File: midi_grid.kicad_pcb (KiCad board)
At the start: 2 copper layers, 275 x 200 mm, 311 parts, among them J1 USB_OTG, J2 3.5mm jack, J3 3.5mm jack, J4 Conn_01x04_Male, Q1 BSS83P, Q10 BSS83P, Q11 BSS83P, Q12 BSS83P, Q13 BSS83P, Q14 BSS83P, Q15 BSS83P, Q16 BSS83P, Q17 BSS83P, Q18 BSS83P, Q19 BSS83P, Q2 BSS83P, Q20 BSS83P, Q21 NX7002AK, Q22 NX7002AK, Q23 NX7002AK, Q24 NX7002AK, Q25 NX7002AK, Q26 NX7002AK, Q27 NX7002AK, Q28 NX7002AK, Q29 NX7002AK, Q3 BSS83P, Q30 NX7002AK, Q31 NX7002AK, Q32 NX7002AK, Q33 NX7002AK, Q34 NX7002AK, Q4 BSS83P, Q5 BSS83P, Q6 BSS83P, Q7 BSS83P, Q8 BSS83P, Q9 BSS83P, SW1 Button_matrix_4x4, SW10 SW_Push, SW11 SW_Push, SW12 SW_Push, SW13 SW_Push, SW14 SW_Push, SW15 SW_Push, SW16 SW_Push, SW17 SW_Push, SW18 SW_Push, SW19 SW_Push, SW2 Button_matrix_4x4, SW20 SW_Push, SW21 SW_Push, SW22 SW_Push, SW23 SW_Push, SW24 SW_Push, SW25 EC12E24204A9, SW26 EC12E24204A9, SW3 Button_matrix_4x4, SW4 Button_matrix_4x4, SW5 SW_Push, SW6 SW_Push, SW7 SW_Push, SW8 SW_Push, SW9 SW_Push, U1 74HC138, U2 74HC138, U3 74HC138, U4 USBUF, U5 STM32F411RCT6, U6 LD1117STR, U7 LTV-357T, Y1 8MHz

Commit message: multiple schematic and pcb changes
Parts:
- removed R35, R36, R37, R38: 10K, Resistors_SMD:R_0603
- added TP1: TEST, Connectors_TestPoints:Test_Point_Pad_d4.0mm, F.Cu at (176.0, 258.5)
- added TP2: TEST, Connectors_TestPoints:Test_Point_Pad_d4.0mm, F.Cu at (182.0, 254.0)
- added TP3: TEST, Connectors_TestPoints:Test_Point_Pad_d4.0mm, F.Cu at (188.5, 255.5)
- added TP4: TEST, Connectors_TestPoints:Test_Point_Pad_d4.0mm, F.Cu at (195.0, 257.0)
- added TP5: TEST, Connectors_TestPoints:Test_Point_Pad_d4.0mm, F.Cu at (201.0, 261.0)
- C14, C15, C2, R52, R53, R54, R55: moved to B.Cu
- moved R28 192.4 mm to (276.0, 96.0), turned to 270 degrees
- moved Q25 188.6 mm to (273.5, 85.5), turned to 180 degrees
- moved R25 187.1 mm to (276.0, 85.5), turned to 270 degrees
- moved R55 178.1 mm to (269.5, 96.0)
- moved Q26 175.0 mm to (273.5, 89.0), turned to 180 degrees
- moved R54 173.8 mm to (269.5, 92.5)
- moved R53 173.3 mm to (269.5, 89.0)
- moved R52 167.7 mm to (269.5, 85.5)
- moved Q28 156.9 mm to (273.5, 96.0), turned to 180 degrees
- moved R27 153.5 mm to (276.0, 92.5), turned to 270 degrees
- moved R26 150.3 mm to (276.0, 89.0), turned to 270 degrees
- moved Q27 149.4 mm to (273.5, 92.5), turned to 180 degrees
- moved C2 136.3 mm to (263.5, 110.5)
- moved C15 102.9 mm to (306.0, 116.0), turned to 270 degrees
- moved C14 101.5 mm to (301.5, 116.0), turned to 270 degrees
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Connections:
- net /grid/BLUE1 renamed /grid/PWM_BLUE1
- net /grid/BLUE2 renamed /grid/PWM_BLUE2
- net /grid/BLUE3 renamed /grid/PWM_BLUE3
- net /grid/BLUE4 renamed /grid/PWM_BLUE4
- net /grid/BUTTON4 renamed /mcu/GRID_BUTTON4
- net /grid/GREEN1 renamed /grid/PWM_GREEN1
- net /grid/GREEN2 renamed /grid/PWM_GREEN2
- net /grid/GREEN3 renamed /grid/PWM_GREEN3
- net /grid/GREEN4 renamed /grid/PWM_GREEN4
- net /mcu/PWM_RED1 renamed /grid/PWM_RED1
- net /mcu/PWM_RED2 renamed /grid/PWM_RED2
- net /mcu/PWM_RED3 renamed /grid/PWM_RED3
- net /mcu/PWM_RED4 renamed /grid/PWM_RED4
- U5 pad 10: /grid/BUTTON3 -> /mcu/GRID_BUTTON3
- U5 pad 2: Net-(U5-Pad2) -> /digital_io/BUTTON2
- U5 pad 24: /digital_io/BUTTON1 -> Net-(TP4-Pad1)
- U5 pad 25: /digital_io/BUTTON2 -> Net-(TP5-Pad1)
- U5 pad 53: Net-(U5-Pad53) -> /digital_io/BUTTON1
- U5 pad 8: /grid/BUTTON1 -> /mcu/GRID_BUTTON1
- U5 pad 9: /grid/BUTTON2 -> /mcu/GRID_BUTTON2
- Y1 pad 2: /mcu/XTAL2 -> GND
- Y1 pad 3: (no net) -> /mcu/XTAL2
- Y1 pad 4: (no net) -> GND
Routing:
- net /mcu/COL3: track 0.00 -> 63.8 mm, vias 0 -> 1
- net /grid/G8: track 1.58 -> 50.0 mm, vias 0 -> 2
- net /grid/G7: track 1.58 -> 48.2 mm, vias 0 -> 2
- net +5V: track 235.4 -> 277.7 mm, vias 2 -> 4
- net /grid/G6: track 1.58 -> 39.9 mm, vias 0 -> 2
- net /grid/G5: track 1.58 -> 36.3 mm, vias 0 -> 2
- net /grid/PWM_GREEN1: track 0.00 -> 17.8 mm
- net /grid/PWM_GREEN2: track 0.00 -> 17.1 mm
- net /grid/PWM_GREEN4: track 0.00 -> 16.4 mm
- net /grid/PWM_GREEN3: track 0.00 -> 16.1 mm
- net /mcu/COL2: track 0.00 -> 8.68 mm
- net /mcu/COL1: track 0.00 -> 8.32 mm
- net (no net): track 0.00 -> 5.00 mm

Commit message: pcb in development
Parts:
- removed TP5: TEST, Connectors_TestPoints:Test_Point_Pad_d4.0mm
- added R35: 10K, Resistors_SMD:R_0603, B.Cu at (295.8, 93.0)
- added TP6: TEST, Connectors_TestPoints:Test_Point_Pad_d3.0mm, F.Cu at (205.0, 259.5)
- C10, C11, C12, C6, C7, C8, C9: moved to B.Cu
- TP1, TP2, TP3: footprint Connectors_TestPoints:Test_Point_Pad_d4.0mm -> Connectors_TestPoints:Test_Point_Pad_d3.0mm
- TP4: footprint Connectors_TestPoints:Test_Point_Pad_d4.0mm -> Connectors_TestPoints:Test_Point_Pad_d3.0mm; moved to B.Cu
- moved TP4 187.9 mm to (280.2, 89.5)
- moved C12 175.3 mm to (296.2, 97.2), turned to 90 degrees
- moved C10 174.2 mm to (308.2, 108.0)
- moved C8 98.0 mm to (304.8, 85.0)
- moved C7 94.2 mm to (304.2, 90.2)
- moved C11 91.6 mm to (300.8, 109.8)
- moved C6 89.8 mm to (297.0, 95.2), turned to 180 degrees
- moved C9 82.0 mm to (307.4, 87.6)
- moved C13 19.4 mm to (367.2, 41.8)
- moved R52 3.50 mm to (269.5, 89.0)
- moved Y1 2.70 mm to (304.2, 113.0)
- moved R53 2.50 mm to (269.5, 91.5)
- moved R54 1.50 mm to (269.5, 94.0)
- moved R55 0.50 mm to (269.5, 96.5)
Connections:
- D10 pad 1: /grid/BUTTON3 -> /grid/GRID_BUTTON3
- D100 pad 1: Net-(D100-Pad1) -> /grid/GRID_BUTTON4
- D102 pad 1: Net-(D100-Pad1) -> /grid/GRID_BUTTON4
- D104 pad 1: Net-(D100-Pad1) -> /grid/GRID_BUTTON4
- D106 pad 1: /grid/BUTTON3 -> /grid/GRID_BUTTON3
- D108 pad 1: /grid/BUTTON3 -> /grid/GRID_BUTTON3
- D110 pad 1: /grid/BUTTON3 -> /grid/GRID_BUTTON3
- D112 pad 1: /grid/BUTTON3 -> /grid/GRID_BUTTON3
- D114 pad 1: /grid/BUTTON2 -> /grid/GRID_BUTTON2
- D116 pad 1: /grid/BUTTON2 -> /grid/GRID_BUTTON2
- D118 pad 1: /grid/BUTTON2 -> /grid/GRID_BUTTON2
- D12 pad 1: /grid/BUTTON3 -> /grid/GRID_BUTTON3
- D120 pad 1: /grid/BUTTON2 -> /grid/GRID_BUTTON2
- D122 pad 1: /grid/BUTTON1 -> /grid/GRID_BUTTON1
- D124 pad 1: /grid/BUTTON1 -> /grid/GRID_BUTTON1
- D126 pad 1: /grid/BUTTON1 -> /grid/GRID_BUTTON1
- D128 pad 1: /grid/BUTTON1 -> /grid/GRID_BUTTON1
- D130 pad 1: Net-(D100-Pad1) -> /grid/GRID_BUTTON4
- D131 pad 1: Net-(D100-Pad1) -> /grid/GRID_BUTTON4
- D133 pad 1: /grid/BUTTON3 -> /grid/GRID_BUTTON3
- D135 pad 1: /grid/BUTTON3 -> /grid/GRID_BUTTON3
- D137 pad 1: /grid/BUTTON2 -> /grid/GRID_BUTTON2
- D138 pad 1: /grid/BUTTON2 -> /grid/GRID_BUTTON2
- D139 pad 1: /grid/BUTTON1 -> /grid/GRID_BUTTON1
- D14 pad 1: /grid/BUTTON3 -> /grid/GRID_BUTTON3
- D141 pad 1: /grid/BUTTON1 -> /grid/GRID_BUTTON1
- D143 pad 1: Net-(D100-Pad1) -> /grid/GRID_BUTTON4
- D145 pad 1: Net-(D100-Pad1) -> /grid/GRID_BUTTON4
- D147 pad 1: /grid/BUTTON3 -> /grid/GRID_BUTTON3
- D149 pad 1: /grid/BUTTON3 -> /grid/GRID_BUTTON3
- D151 pad 1: /grid/BUTTON2 -> /grid/GRID_BUTTON2
- D153 pad 1: /grid/BUTTON2 -> /grid/GRID_BUTTON2
- D155 pad 1: /grid/BUTTON1 -> /grid/GRID_BUTTON1
- D157 pad 1: /grid/BUTTON1 -> /grid/GRID_BUTTON1
- D16 pad 1: /grid/BUTTON3 -> /grid/GRID_BUTTON3
- D18 pad 1: /grid/BUTTON2 -> /grid/GRID_BUTTON2
- D2 pad 1: Net-(D100-Pad1) -> /grid/GRID_BUTTON4
- D20 pad 1: /grid/BUTTON2 -> /grid/GRID_BUTTON2
- D22 pad 1: /grid/BUTTON2 -> /grid/GRID_BUTTON2
- D24 pad 1: /grid/BUTTON2 -> /grid/GRID_BUTTON2
- D26 pad 1: /grid/BUTTON1 -> /grid/GRID_BUTTON1
- D28 pad 1: /grid/BUTTON1 -> /grid/GRID_BUTTON1
- D30 pad 1: /grid/BUTTON1 -> /grid/GRID_BUTTON1
- D32 pad 1: /grid/BUTTON1 -> /grid/GRID_BUTTON1
- D34 pad 1: Net-(D100-Pad1) -> /grid/GRID_BUTTON4
- D36 pad 1: Net-(D100-Pad1) -> /grid/GRID_BUTTON4
- D38 pad 1: Net-(D100-Pad1) -> /grid/GRID_BUTTON4
- D4 pad 1: Net-(D100-Pad1) -> /grid/GRID_BUTTON4
- D40 pad 1: Net-(D100-Pad1) -> /grid/GRID_BUTTON4
- D42 pad 1: /grid/BUTTON3 -> /grid/GRID_BUTTON3
- D44 pad 1: /grid/BUTTON3 -> /grid/GRID_BUTTON3
- D46 pad 1: /grid/BUTTON3 -> /grid/GRID_BUTTON3
- D48 pad 1: /grid/BUTTON3 -> /grid/GRID_BUTTON3
- D50 pad 1: /grid/BUTTON2 -> /grid/GRID_BUTTON2
- D52 pad 1: /grid/BUTTON2 -> /grid/GRID_BUTTON2
- D54 pad 1: /grid/BUTTON2 -> /grid/GRID_BUTTON2
- D56 pad 1: /grid/BUTTON2 -> /grid/GRID_BUTTON2
- D58 pad 1: /grid/BUTTON1 -> /grid/GRID_BUTTON1
- D6 pad 1: Net-(D100-Pad1) -> /grid/GRID_BUTTON4
- D60 pad 1: /grid/BUTTON1 -> /grid/GRID_BUTTON1
- D62 pad 1: /grid/BUTTON1 -> /grid/GRID_BUTTON1
- D64 pad 1: /grid/BUTTON1 -> /grid/GRID_BUTTON1
- D66 pad 1: Net-(D100-Pad1) -> /grid/GRID_BUTTON4
- D68 pad 1: Net-(D100-Pad1) -> /grid/GRID_BUTTON4
- D70 pad 1: Net-(D100-Pad1) -> /grid/GRID_BUTTON4
- D72 pad 1: Net-(D100-Pad1) -> /grid/GRID_BUTTON4
- D74 pad 1: /grid/BUTTON3 -> /grid/GRID_BUTTON3
- D76 pad 1: /grid/BUTTON3 -> /grid/GRID_BUTTON3
- D78 pad 1: /grid/BUTTON3 -> /grid/GRID_BUTTON3
- D8 pad 1: Net-(D100-Pad1) -> /grid/GRID_BUTTON4
- D80 pad 1: /grid/BUTTON3 -> /grid/GRID_BUTTON3
- D82 pad 1: /grid/BUTTON2 -> /grid/GRID_BUTTON2
- D84 pad 1: /grid/BUTTON2 -> /grid/GRID_BUTTON2
- D86 pad 1: /grid/BUTTON2 -> /grid/GRID_BUTTON2
- D88 pad 1: /grid/BUTTON2 -> /grid/GRID_BUTTON2
- D90 pad 1: /grid/BUTTON1 -> /grid/GRID_BUTTON1
- D92 pad 1: /grid/BUTTON1 -> /grid/GRID_BUTTON1
- D94 pad 1: /grid/BUTTON1 -> /grid/GRID_BUTTON1
- D96 pad 1: /grid/BUTTON1 -> /grid/GRID_BUTTON1
- D98 pad 1: Net-(D100-Pad1) -> /grid/GRID_BUTTON4
- U5 pad 10: /mcu/GRID_BUTTON3 -> /grid/GRID_BUTTON3
- U5 pad 11: /mcu/GRID_BUTTON4 -> /grid/GRID_BUTTON4
- U5 pad 2: /digital_io/BUTTON2 -> /digital_io/BUTTON1
- U5 pad 28: Net-(U5-Pad28) -> /digital_io/LCD_RESET
- U5 pad 29: /digital_io/LCD_DC -> /digital_io/LCD_CS
- U5 pad 3: /digital_io/ROTARY2_A -> /digital_io/ROTARY1_A
- U5 pad 33: /digital_io/LCD_CS -> /digital_io/LCD_DC
- U5 pad 39: /digital_io/LCD_RESET -> Net-(TP6-Pad1)
- U5 pad 4: /digital_io/ROTARY2_B -> /digital_io/ROTARY1_B
- U5 pad 51: /digital_io/ROTARY1_A -> /digital_io/ROTARY2_A
- U5 pad 52: /digital_io/ROTARY1_B -> /digital_io/ROTARY2_B
- U5 pad 53: /digital_io/BUTTON1 -> /digital_io/BUTTON2
- U5 pad 8: /mcu/GRID_BUTTON1 -> /grid/GRID_BUTTON1
- U5 pad 9: /mcu/GRID_BUTTON2 -> /grid/GRID_BUTTON2
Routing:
- net /grid/GRID_BUTTON1: track 0.00 -> 511.3 mm, vias 0 -> 3
- net /grid/BUTTON1: track 508.0 -> 0.00 mm, vias 3 -> 0
- net /grid/GRID_BUTTON3: track 0.00 -> 499.2 mm, vias 0 -> 3
- net /grid/BUTTON3: track 495.9 -> 0.00 mm, vias 3 -> 0
- net /grid/GRID_BUTTON2: track 0.00 -> 475.9 mm, vias 0 -> 3
- net /grid/BUTTON2: track 472.6 -> 0.00 mm, vias 3 -> 0
- net /grid/GRID_BUTTON4: track 0.00 -> 462.9 mm, vias 0 -> 3
- net Net-(D100-Pad1): track 459.6 -> 0.00 mm, vias 3 -> 0
- net GND: track 0.75 -> 26.7 mm, vias 1 -> 2
- net Net-(TP4-Pad1): track 0.00 -> 17.4 mm
- net /grid/PWM_GREEN1: track 17.8 -> 32.8 mm
- net /digital_io/LCD_RESET: track 0.00 -> 12.1 mm
- net /grid/PWM_GREEN2: track 17.1 -> 28.6 mm
- net /digital_io/LCD_CS: track 0.00 -> 8.71 mm
- net +3V3: track 8.59 -> 16.3 mm, vias 0 -> 1
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
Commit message: pcb development
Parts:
- Q33, R34, R60: moved to F.Cu
- R48, R49, R50, R51: moved to B.Cu
- moved R24 199.4 mm to (276.0, 96.0), turned to 270 degrees
- moved R49 172.9 mm to (269.5, 91.5)
- moved R51 172.6 mm to (269.5, 96.5)
- moved R48 171.2 mm to (269.5, 89.0)
- moved R50 170.3 mm to (269.5, 94.0)
- moved Q21 165.5 mm to (273.5, 85.5), turned to 180 degrees
- moved Q24 153.1 mm to (273.5, 96.0), turned to 180 degrees
- moved Q23 150.6 mm to (273.5, 92.5), turned to 180 degrees
- moved R22 150.1 mm to (276.0, 89.0), turned to 270 degrees
- moved R21 146.8 mm to (276.0, 85.5), turned to 270 degrees
- moved R23 145.0 mm to (276.0, 92.5), turned to 270 degrees
- moved Q22 142.4 mm to (273.5, 89.0), turned to 180 degrees
- moved U4 45.2 mm to (338.0, 91.5)
- moved Q25 25.0 mm to (273.2, 60.5)
- moved Q26 25.0 mm to (273.2, 64.0)
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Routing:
- net Net-(D121-Pad1): track 530.6 -> 683.8 mm, vias 0 -> 3
- net Net-(D1-Pad1): track 451.3 -> 587.3 mm, vias 0 -> 3
- net Net-(D105-Pad1): track 488.4 -> 620.5 mm, vias 0 -> 3
- net Net-(D113-Pad1): track 463.5 -> 569.9 mm, vias 0 -> 2
- net /mcu/USB_DP: track 0.00 -> 55.5 mm
- net /mcu/USB_DM: track 0.00 -> 54.9 mm
- net /grid/PWM_GREEN4: track 16.9 -> 51.9 mm
- net /grid/PWM_RED4: track 0.00 -> 34.5 mm
- net /grid/PWM_GREEN3: track 18.2 -> 52.0 mm
- net /grid/PWM_RED2: track 2.32 -> 34.6 mm
- net /grid/PWM_RED3: track 1.71 -> 33.0 mm
- net /grid/PWM_RED1: track 5.75 -> 36.3 mm
- net Net-(TP4-Pad1): track 17.4 -> 47.9 mm
- net GND: track 26.7 -> 53.7 mm, vias 2 -> 3
- net /mcu/USB_M: track 0.00 -> 25.9 mm, vias 0 -> 1
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
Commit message: commiting before bulk led schematic symbol change
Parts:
- C13, C3, R56, R57, R58, R59: moved to B.Cu
- R45: moved to F.Cu
- moved R58 242.0 mm to (397.2, 140.0)
- moved R57 241.8 mm to (397.5, 135.8)
- moved R56 222.5 mm to (397.8, 131.2)
- moved R59 196.7 mm to (397.2, 144.2)
- moved R45 138.9 mm to (305.0, 64.0)
- moved R33 108.7 mm to (347.0, 108.0)
- moved C13 93.9 mm to (296.2, 103.2), turned to 180 degrees
- moved C3 84.0 mm to (376.8, 80.8)
- moved R32 83.3 mm to (390.0, 144.5), turned to 90 degrees
- moved R31 81.8 mm to (390.0, 140.5), turned to 90 degrees
- moved R29 81.1 mm to (390.0, 131.5), turned to 90 degrees
- moved U3 78.1 mm to (378.8, 84.5)
- moved R30 77.9 mm to (390.0, 136.0), turned to 90 degrees
- moved SW22 58.8 mm to (295.0, 109.0), turned to 270 degrees
- moved Q32 58.7 mm to (392.5, 144.5)
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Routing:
- net Net-(D121-Pad4): track 536.3 -> 766.5 mm, vias 0 -> 3
- net Net-(D113-Pad4): track 468.9 -> 681.5 mm, vias 0 -> 3
- net Net-(D105-Pad4): track 492.1 -> 681.5 mm, vias 0 -> 3
- net Net-(D1-Pad4): track 456.8 -> 642.9 mm, vias 0 -> 3
- net /mcu/NRST: track 6.86 -> 10.9 mm
- net /digital_io/LCD_LIGHT: track 8.15 -> 10.9 mm
- net /grid/GRID_BUTTON2: track 478.7 -> 480.3 mm
- net /grid/GRID_BUTTON3: track 501.2 -> 502.5 mm
- net Net-(D105-Pad1): track 620.5 -> 621.2 mm
- net (no net): vias 6 -> 0

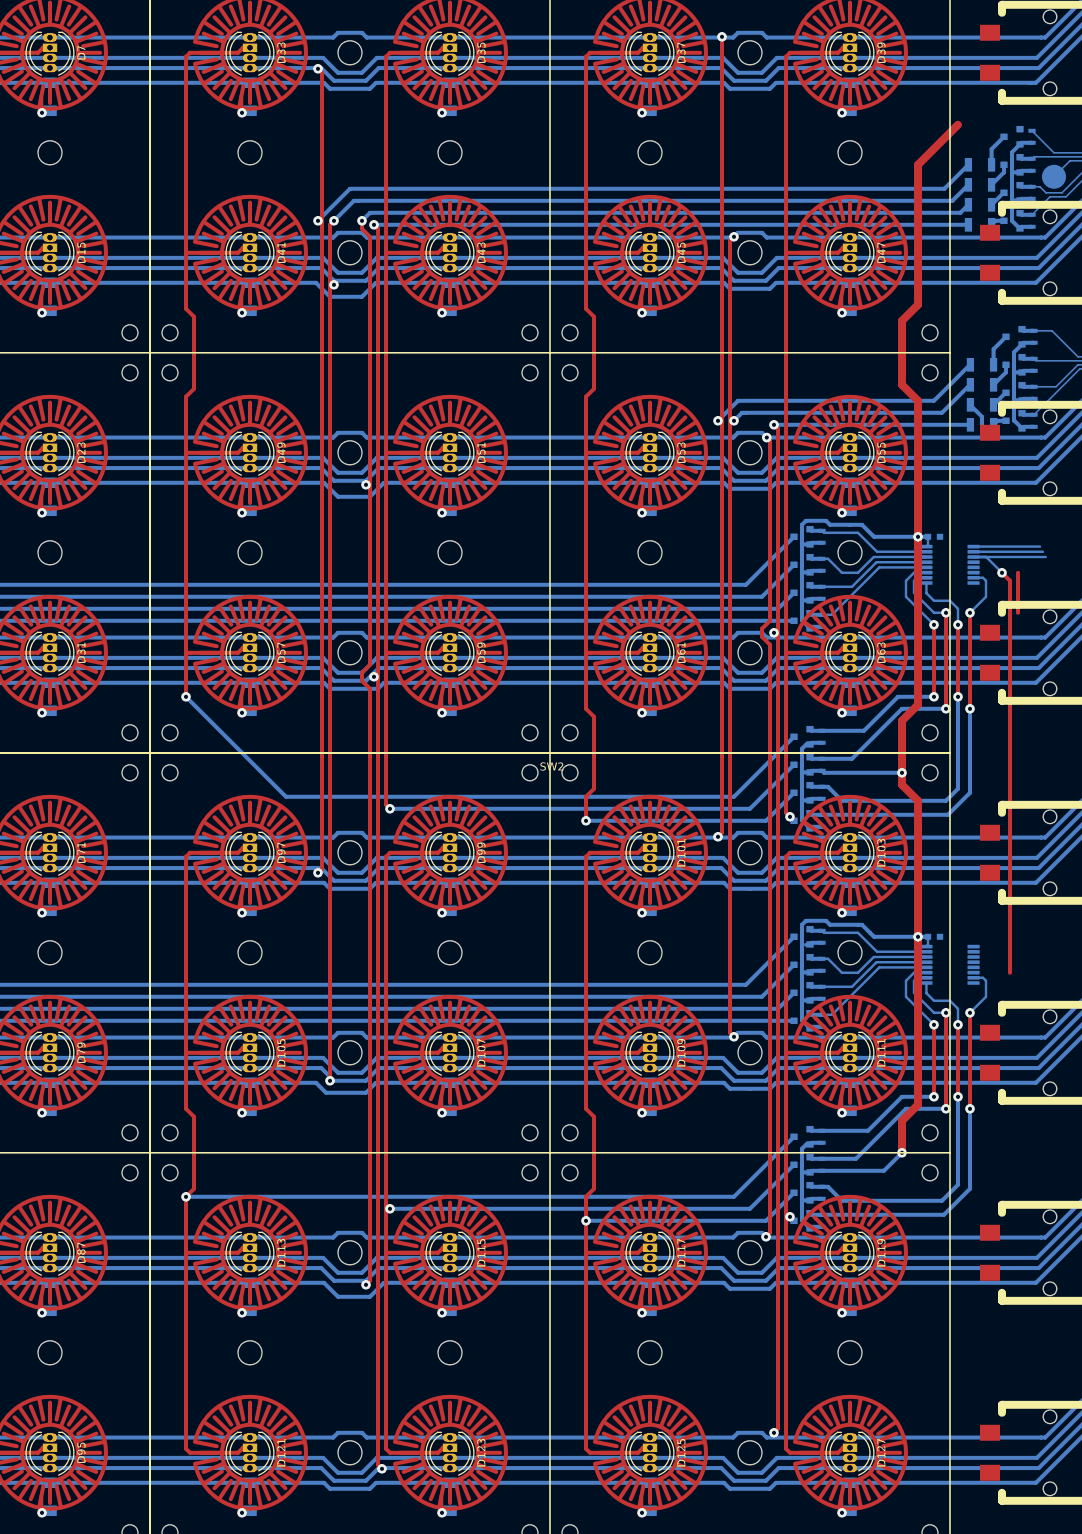
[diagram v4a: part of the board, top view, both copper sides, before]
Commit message: successfuly changed component symbols and net names, further developed pcb
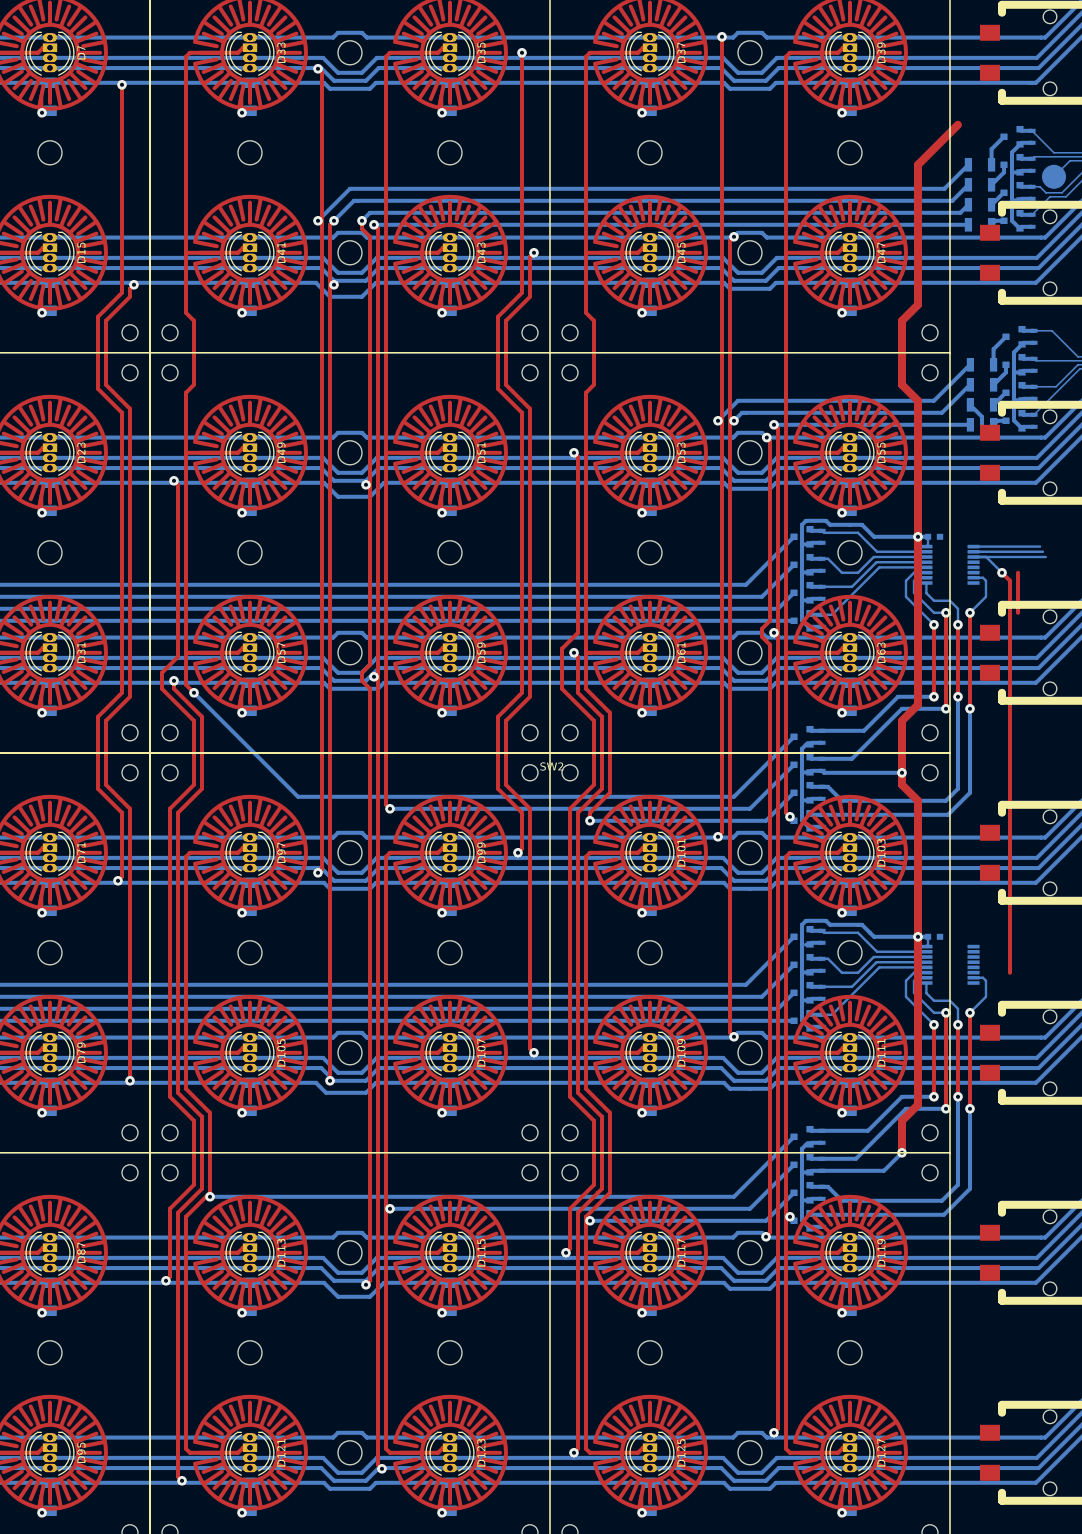
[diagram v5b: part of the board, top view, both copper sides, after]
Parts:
- D1, D101, D103, D105, D107, D109, D11, D111, D113, D115, D117, D119, D121, D123, D125, D127, D129, D13, D132, D134, D136, D140, D142, D144, D146, D148, D15, D150, D152, D154, D156, D17, D19, D21, D23, D25, D27, D29, D3, D31, D33, D35, D37, D39, D41, D43, D45, D47, D49, D5, D51, D53, D55, D57, D59, D61, D63, D65, D67, D69, D7, D71, D73, D75, D77, D79, D81, D83, D85, D87, D89, D9, D91, D93, D95, D97, D99: value LED_RABG -> LED_RAGB
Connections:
- Q25 pad 1: /grid/PWM_GREEN4 -> /grid/PWM_BLUE4
- Q26 pad 1: /grid/PWM_GREEN3 -> /grid/PWM_BLUE3
- Q27 pad 1: /grid/PWM_GREEN2 -> /grid/PWM_BLUE2
- Q28 pad 1: /grid/PWM_GREEN1 -> /grid/PWM_BLUE1
- Q29 pad 1: /grid/PWM_BLUE4 -> /grid/PWM_GREEN4
- Q30 pad 1: /grid/PWM_BLUE3 -> /grid/PWM_GREEN3
- Q31 pad 1: /grid/PWM_BLUE2 -> /grid/PWM_GREEN2
- Q32 pad 1: /grid/PWM_BLUE1 -> /grid/PWM_GREEN1
- R25 pad 1: /grid/PWM_GREEN4 -> /grid/PWM_BLUE4
- R26 pad 1: /grid/PWM_GREEN3 -> /grid/PWM_BLUE3
- R27 pad 1: /grid/PWM_GREEN2 -> /grid/PWM_BLUE2
- R28 pad 1: /grid/PWM_GREEN1 -> /grid/PWM_BLUE1
- R29 pad 1: /grid/PWM_BLUE4 -> /grid/PWM_GREEN4
- R30 pad 1: /grid/PWM_BLUE3 -> /grid/PWM_GREEN3
- R31 pad 1: /grid/PWM_BLUE2 -> /grid/PWM_GREEN2
- R32 pad 1: /grid/PWM_BLUE1 -> /grid/PWM_GREEN1
- U5 pad 22: /grid/PWM_GREEN1 -> /grid/PWM_BLUE1
- U5 pad 23: /grid/PWM_GREEN2 -> /grid/PWM_BLUE2
- U5 pad 26: /grid/PWM_GREEN3 -> /grid/PWM_BLUE3
- U5 pad 27: /grid/PWM_GREEN4 -> /grid/PWM_BLUE4
- U5 pad 58: /grid/PWM_BLUE1 -> /grid/PWM_GREEN1
- U5 pad 59: /grid/PWM_BLUE2 -> /grid/PWM_GREEN2
- U5 pad 61: /grid/PWM_BLUE3 -> /grid/PWM_GREEN3
- U5 pad 62: /grid/PWM_BLUE4 -> /grid/PWM_GREEN4
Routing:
- net Net-(D113-Pad3): track 470.7 -> 578.9 mm, vias 0 -> 2
- net Net-(D105-Pad3): track 493.9 -> 600.9 mm, vias 0 -> 2
- net /grid/GRID_BUTTON2: track 480.3 -> 587.2 mm, vias 3 -> 5
- net Net-(D121-Pad3): track 538.1 -> 644.8 mm, vias 0 -> 2
- net Net-(D1-Pad3): track 458.6 -> 565.0 mm, vias 0 -> 2
- net /grid/GRID_BUTTON1: track 514.4 -> 620.8 mm, vias 3 -> 5
- net /grid/GRID_BUTTON4: track 464.6 -> 570.0 mm, vias 3 -> 5
- net /grid/GRID_BUTTON3: track 502.5 -> 607.4 mm, vias 3 -> 5
- net /grid/PWM_BLUE4: track 0.00 -> 53.5 mm
- net /grid/PWM_GREEN1: track 53.1 -> 0.00 mm
- net /grid/PWM_BLUE1: track 0.00 -> 53.1 mm
- net /grid/PWM_GREEN2: track 52.7 -> 0.00 mm
- net /grid/PWM_BLUE2: track 0.00 -> 52.7 mm
- net /grid/PWM_GREEN3: track 52.0 -> 0.00 mm
- net /grid/PWM_BLUE3: track 0.00 -> 52.0 mm
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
